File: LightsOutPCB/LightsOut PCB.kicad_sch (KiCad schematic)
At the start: 34 parts, among them J1 Power, J2 Digital/PWM, J3 Analog, J4 Digital/PWM, J5 Conn_01x04_Pin, SW1 B3W-4050, SW2 B3W-4050, U1 SN74HC595N

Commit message: finished initial placement
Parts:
- LED6, LED7, LED8, LED9: footprint PCM_LED_THT_AKL:LED_D5.0mm -> LED_THT_AKL_Double:LED_D5.0mm
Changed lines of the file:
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@@
 			)
 		)
-		(property "Footprint" "PCM_LED_THT_AKL:LED_D5.0mm"
+		(property "Footprint" "LED_THT_AKL_Double:LED_D5.0mm"
 			(at 220.98 44.45 0)
 			(hide yes)
@@
 		)
 		(property "Description" "Green LED, 5mm THT, Alternate KiCad Library"
+			(at 220.98 44.45 0)
+			(hide yes)
+			(show_name no)
+			(do_not_autoplace no)
+			(effects
+				(font
+					(size 1.27 1.27)
+				)
+			)
+		)
+		(property "Functionality Text" ""
 			(at 220.98 44.45 0)
 			(hide yes)
@@
 			)
 		)
-		(property "Footprint" "PCM_LED_THT_AKL:LED_D5.0mm"
+		(property "Footprint" "LED_THT_AKL_Double:LED_D5.0mm"
 			(at 220.98 73.66 0)
 			(hide yes)
@@
 			)
 		)
-		(property "Footprint" "PCM_LED_THT_AKL:LED_D5.0mm"
+		(property "Footprint" "LED_THT_AKL_Double:LED_D5.0mm"
 			(at 220.98 87.63 0)
 			(hide yes)
@@
 			)
 		)
-		(property "Footprint" "PCM_LED_THT_AKL:LED_D5.0mm"
+		(property "Footprint" "LED_THT_AKL_Double:LED_D5.0mm"
 			(at 220.98 58.42 0)
 			(hide yes)

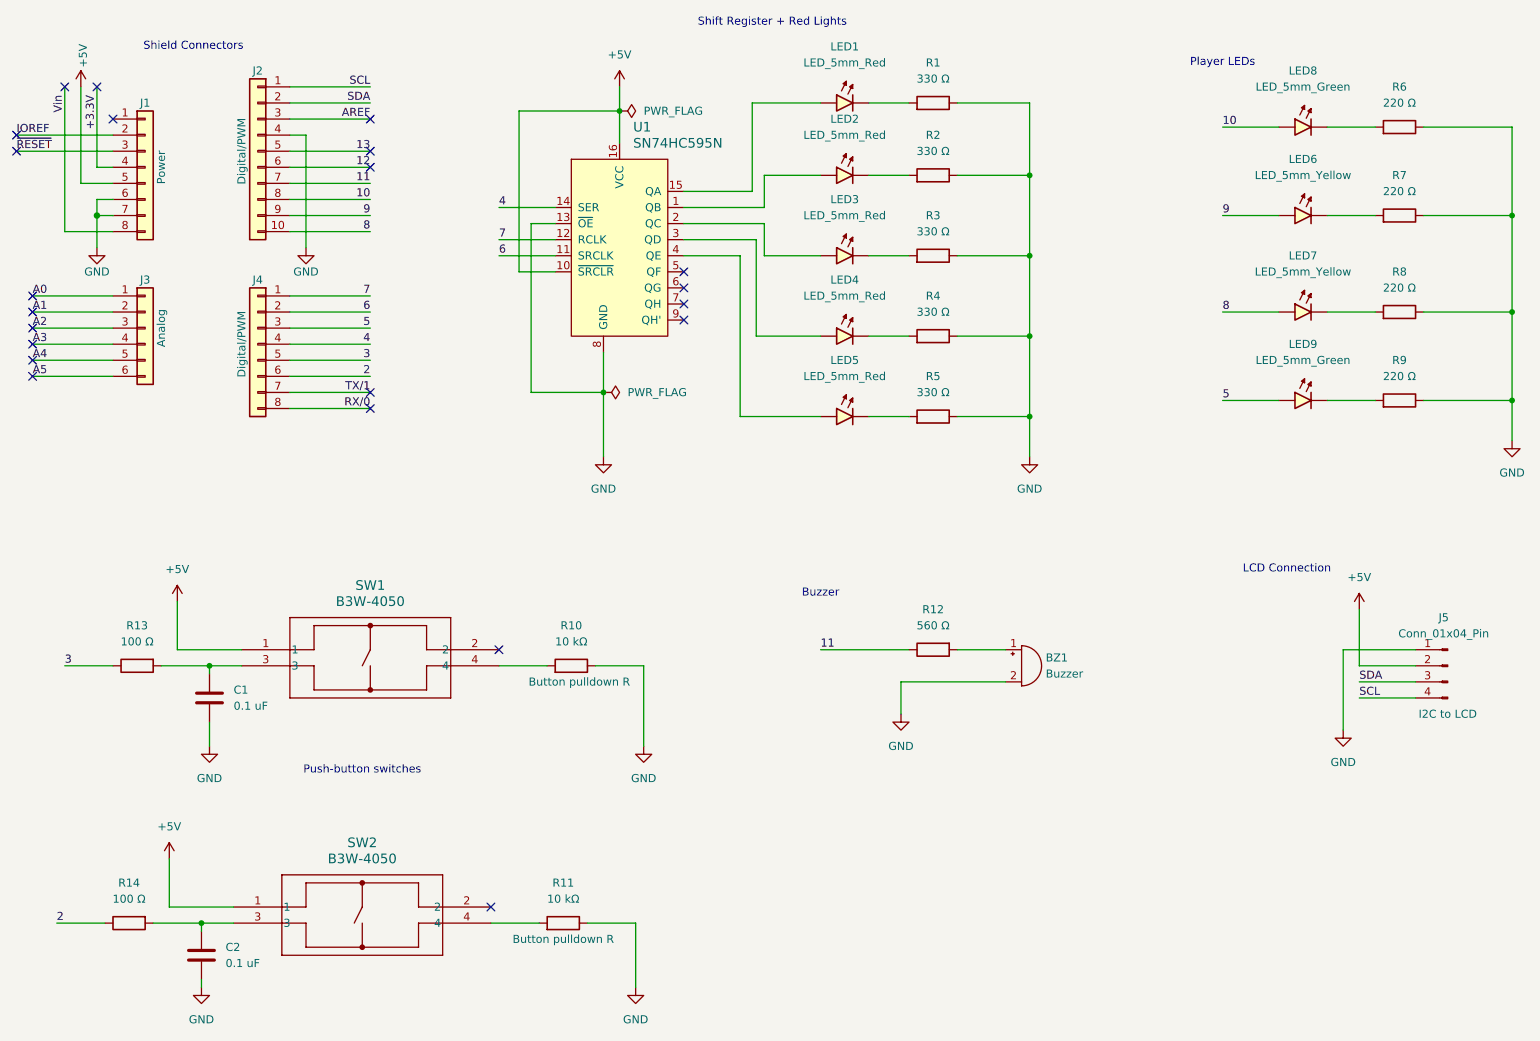
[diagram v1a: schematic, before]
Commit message: info on front silkscreen
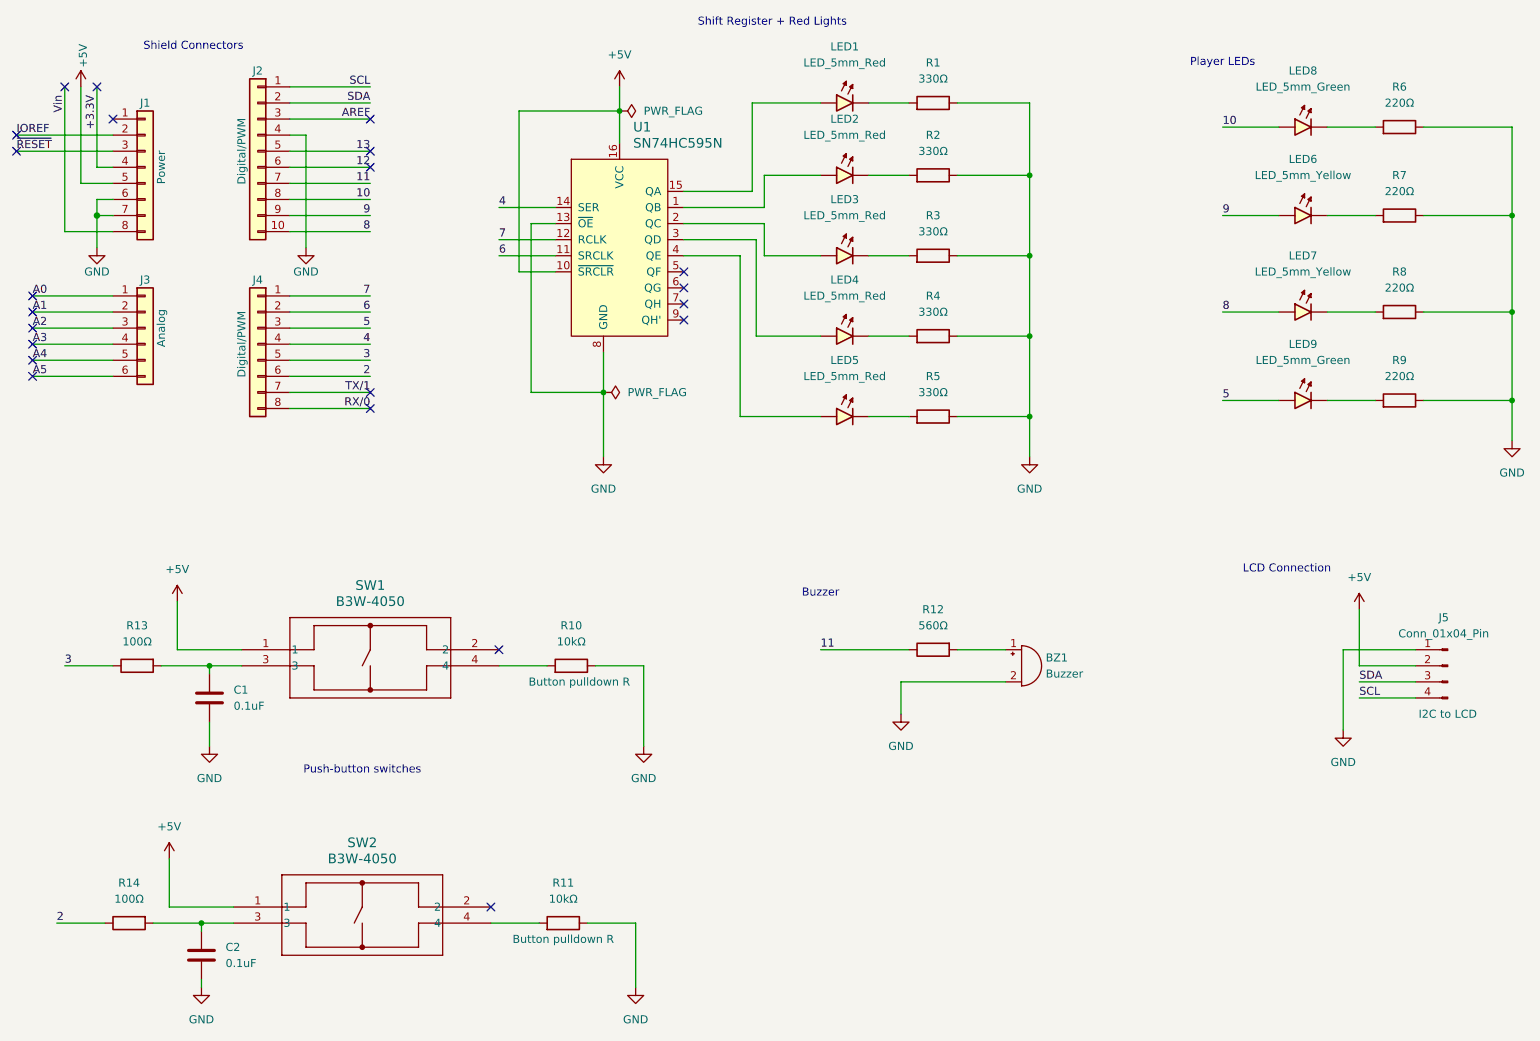
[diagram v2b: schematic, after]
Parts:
- C1, C2: value 0.1 uF -> 0.1uF
- R1, R2, R3, R4, R5: value 330 Ω -> 330Ω
- R10, R11: value 10 kΩ -> 10kΩ
- R12: value 560 Ω -> 560Ω
- R13, R14: value 100 Ω -> 100Ω
- R6, R7, R8, R9: value 220 Ω -> 220Ω
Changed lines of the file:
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@@
 			)
 		)
-		(property "Value" "10 kΩ"
+		(property "Value" "10kΩ"
 			(at 104.14 166.37 90)
 			(show_name no)
@@
 			)
 		)
-		(property "Value" "100 Ω"
+		(property "Value" "100Ω"
 			(at 36.83 125.73 90)
 			(show_name no)
@@
 			)
 		)
-		(property "Value" "220 Ω"
+		(property "Value" "220Ω"
 			(at 236.22 69.85 90)
 			(show_name no)
@@
 			)
 		)
-		(property "Value" "220 Ω"
+		(property "Value" "220Ω"
 			(at 236.22 40.64 90)
 			(show_name no)
@@
 			)
 		)
-		(property "Value" "560 Ω"
+		(property "Value" "560Ω"
 			(at 162.56 123.19 90)
 			(show_name no)
@@
 			)
 		)
-		(property "Value" "100 Ω"
+		(property "Value" "100Ω"
 			(at 35.56 166.37 90)
 			(show_name no)
@@
 			)
 		)
-		(property "Value" "330 Ω"
+		(property "Value" "330Ω"
 			(at 162.56 48.26 90)
 			(show_name no)
@@
 			)
 		)
-		(property "Value" "330 Ω"
+		(property "Value" "330Ω"
 			(at 162.56 73.66 90)
 			(show_name no)
@@
 			)
 		)
-		(property "Value" "10 kΩ"
+		(property "Value" "10kΩ"
 			(at 105.41 125.73 90)
 			(show_name no)
@@
 			)
 		)
-		(property "Value" "330 Ω"
+		(property "Value" "330Ω"
 			(at 162.56 36.83 90)
 			(show_name no)
@@
 			)
 		)
-		(property "Value" "0.1 uF"
+		(property "Value" "0.1uF"
 			(at 52.07 135.8899 0)
 			(show_name no)
@@
 			)
 		)
-		(property "Value" "330 Ω"
+		(property "Value" "330Ω"
 			(at 162.56 86.36 90)
 			(show_name no)
@@
 			)
 		)
-		(property "Value" "220 Ω"
+		(property "Value" "220Ω"
 			(at 236.22 54.61 90)
 			(show_name no)
@@
 			)
 		)
-		(property "Value" "220 Ω"
+		(property "Value" "220Ω"
 			(at 236.22 83.82 90)
 			(show_name no)
@@
 			)
 		)
-		(property "Value" "330 Ω"
+		(property "Value" "330Ω"
 			(at 162.56 60.96 90)
 			(show_name no)
@@
 			)
 		)
-		(property "Value" "0.1 uF"
+		(property "Value" "0.1uF"
 			(at 50.8 176.5299 0)
 			(show_name no)
